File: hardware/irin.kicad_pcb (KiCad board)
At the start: 2 copper layers, 12 parts, among them J1 Battery terminals, U1 MP1584EN set to 5.0V, U2 01Space ESP32-C3-0.42LCD, U3 HiLetgo ADS1115 (0x48, ADDR->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, U4 DHT-22

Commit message: Rename project to Irin
Irin (Aramaic ʿirin, "watchers", "the wakeful ones") from the Book of
Enoch; the name's root is documented in README.md and CLAUDE.md.

- KiCad project hardware/irin.*, footprint library Uncharted -> Irin;
  ERC unchanged, regenerated netlist equivalent, preview.pdf refreshed
- Firmware config esphome/irin.yaml, dashboard ha_config/dashboard.yaml
- Breadboard generator points at irin.net; regenerated, validates OK
- The "Uncharted 12V" instance keeps its device name, entity IDs and
  secrets keys so existing HA entities and history are untouched

Co-Authored-By: Claude Opus 5.5 <noreply@anthropic.com>
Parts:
- U1: footprint Uncharted:MP1584EN_HW133_2x2Pad_P2.54mm_W7.62mm_L17.78mm -> Irin:MP1584EN_HW133_2x2Pad_P2.54mm_W7.62mm_L17.78mm
- U2: footprint Uncharted:ESP32C3_042LCD_2x8_P2.54mm_W17.78mm -> Irin:ESP32C3_042LCD_2x8_P2.54mm_W17.78mm
- U3: footprint Uncharted:ADS1115_HiLetgo_1x10_P2.54mm_W18mm_L28.3mm -> Irin:ADS1115_HiLetgo_1x10_P2.54mm_W18mm_L28.3mm
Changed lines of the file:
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@@
 		)
 	)
-	(footprint "Uncharted:MP1584EN_HW133_2x2Pad_P2.54mm_W7.62mm_L17.78mm"
+	(footprint "Irin:MP1584EN_HW133_2x2Pad_P2.54mm_W7.62mm_L17.78mm"
 		(layer "F.Cu")
 		(at 22.987 64.8208)
-		(descr "MP1584EN adjustable buck module, HW-133A~F clone (silkscreen: 降压模块 / 输入 / 输出). 4 nets, each broken out to 2 redundant through-holes at 0.1in pitch: VIN-/VIN+ on one edge, VOUT-/VOUT+ on the opposite edge, 0.7in apart; the two net pairs on each edge are 0.3in apart center-to-center. Measured by owner with a ruler (input/output edge spacing and pair pitch only -- +/-0.5mm). Board outline below is NOT measured -- it is a generous placeholder box around the hole pattern for visual reference only. Pad numbers match the Uncharted:BUCK_MODULE schematic symbol (1=IN+ 2=IN- 3=OUT+ 4=OUT-). Rectangular pads mark the '+' nets (IN+, OUT+), matching the square pads printed on the real board next to its own '+' silkscreen -- also serves as the footprint's pin-1 indicator.")
+		(descr "MP1584EN adjustable buck module, HW-133A~F clone (silkscreen: 降压模块 / 输入 / 输出). 4 nets, each broken out to 2 redundant through-holes at 0.1in pitch: VIN-/VIN+ on one edge, VOUT-/VOUT+ on the opposite edge, 0.7in apart; the two net pairs on each edge are 0.3in apart center-to-center. Measured by owner with a ruler (input/output edge spacing and pair pitch only -- +/-0.5mm). Board outline below is NOT measured -- it is a generous placeholder box around the hole pattern for visual reference only. Pad numbers match the Irin:BUCK_MODULE schematic symbol (1=IN+ 2=IN- 3=OUT+ 4=OUT-). Rectangular pads mark the '+' nets (IN+, OUT+), matching the square pads printed on the real board next to its own '+' silkscreen -- also serves as the footprint's pin-1 indicator.")
 		(tags "MP1584EN HW-133 buck module perfboard")
 		(property "Reference" "U1"
@@
 		)
 		(sheetname "/")
-		(sheetfile "uncharted-battery-monitor.kicad_sch")
+		(sheetfile "irin.kicad_sch")
 		(units
 			(unit
@@
 		)
 		(sheetname "/")
-		(sheetfile "uncharted-battery-monitor.kicad_sch")
+		(sheetfile "irin.kicad_sch")
 		(units
 			(unit
@@
 		)
 	)
-	(footprint "Uncharted:ESP32C3_042LCD_2x8_P2.54mm_W17.78mm"
+	(footprint "Irin:ESP32C3_042LCD_2x8_P2.54mm_W17.78mm"
 		(layer "F.Cu")
 		(at 34.5948 57.2008)
-		(descr "01Space ESP32-C3-0.42LCD dev board: 2x8 THT pin rows, 0.1in pitch, 0.7in row spacing. Pad numbers match the Uncharted:ESP32C3_BOARD schematic symbol (1=5V 2=3V3 3=GND 4=GPIO3 5=GPIO5 6=GPIO6); pads 7-16 are the board's other physical pins, not used in this design, numbered arbitrarily.")
+		(descr "01Space ESP32-C3-0.42LCD dev board: 2x8 THT pin rows, 0.1in pitch, 0.7in row spacing. Pad numbers match the Irin:ESP32C3_BOARD schematic symbol (1=5V 2=3V3 3=GND 4=GPIO3 5=GPIO5 6=GPIO6); pads 7-16 are the board's other physical pins, not used in this design, numbered arbitrarily.")
 		(tags "ESP32-C3 01Space 0.42LCD perfboard")
 		(property "Reference" "U2"
@@
 		)
 		(sheetname "/")
-		(sheetfile "uncharted-battery-monitor.kicad_sch")
+		(sheetfile "irin.kicad_sch")
 		(units
 			(unit
@@
 		)
 		(sheetname "/")
-		(sheetfile "uncharted-battery-monitor.kicad_sch")
+		(sheetfile "irin.kicad_sch")
 		(units
 			(unit
@@
 		)
 		(sheetname "/")
-		(sheetfile "uncharted-battery-monitor.kicad_sch")
+		(sheetfile "irin.kicad_sch")
 		(units
 			(unit
@@
 		)
 		(sheetname "/")
-		(sheetfile "uncharted-battery-monitor.kicad_sch")
+		(sheetfile "irin.kicad_sch")
 		(units
 			(unit
@@
 		)
 	)
-	(footprint "Uncharted:ADS1115_HiLetgo_1x10_P2.54mm_W18mm_L28.3mm"
+	(footprint "Irin:ADS1115_HiLetgo_1x10_P2.54mm_W18mm_L28.3mm"
 		(layer "F.Cu")
 		(at 70.9732 63.0682 -90)
-		(descr "HiLetgo ADS1115 16-bit ADC breakout (ASIN B07VPFLSMX). Single row of 10 THT pins at 0.1in (2.54mm) pitch along one long edge. Board outline 28.3mm x 18mm is from the published listing spec, NOT measured by owner -- drawn as a generous placeholder box for visual reference only, same caveat as Uncharted:MP1584EN_HW133. Pin ROW ORDER is CONFIRMED by owner against the physical module's silkscreen as VDD GND SCL SDA ADDR ALRT A0 A1 A2 A3 (left to right). Pad numbers match the Uncharted:ADS1115 schematic symbol (1=VDD 2=GND 3=SCL 4=SDA 5=ADDR 6=A0); pads 7,9,10 are the module's other physical pins (ALRT, A1, A2, A3) not used in this design, numbered arbitrarily. The module is cable-wired to the ESP32's Qwiic port rather than pin-header-mounted (see CLAUDE.md).")
+		(descr "HiLetgo ADS1115 16-bit ADC breakout (ASIN B07VPFLSMX). Single row of 10 THT pins at 0.1in (2.54mm) pitch along one long edge. Board outline 28.3mm x 18mm is from the published listing spec, NOT measured by owner -- drawn as a generous placeholder box for visual reference only, same caveat as Irin:MP1584EN_HW133. Pin ROW ORDER is CONFIRMED by owner against the physical module's silkscreen as VDD GND SCL SDA ADDR ALRT A0 A1 A2 A3 (left to right). Pad numbers match the Irin:ADS1115 schematic symbol (1=VDD 2=GND 3=SCL 4=SDA 5=ADDR 6=A0); pads 7,9,10 are the module's other physical pins (ALRT, A1, A2, A3) not used in this design, numbered arbitrarily. The module is cable-wired to the ESP32's Qwiic port rather than pin-header-mounted (see CLAUDE.md).")
 		(tags "ADS1115 HiLetgo ADC breakout perfboard")
 		(property "Reference" "U3"
@@
 		)
 		(sheetname "/")
-		(sheetfile "uncharted-battery-monitor.kicad_sch")
+		(sheetfile "irin.kicad_sch")
 		(units
 			(unit
@@
 		)
 		(sheetname "/")
-		(sheetfile "uncharted-battery-monitor.kicad_sch")
+		(sheetfile "irin.kicad_sch")
 		(units
 			(unit
@@
 		)
 		(sheetname "/")
-		(sheetfile "uncharted-battery-monitor.kicad_sch")
+		(sheetfile "irin.kicad_sch")
 		(units
 			(unit
@@
 		)
 		(sheetname "/")
-		(sheetfile "uncharted-battery-monitor.kicad_sch")
+		(sheetfile "irin.kicad_sch")
 		(units
 			(unit
@@
 		)
 		(sheetname "/")
-		(sheetfile "uncharted-battery-monitor.kicad_sch")
+		(sheetfile "irin.kicad_sch")
 		(units
 			(unit
@@
 		)
 		(sheetname "/")
-		(sheetfile "uncharted-battery-monitor.kicad_sch")
+		(sheetfile "irin.kicad_sch")
 		(units
 			(unit

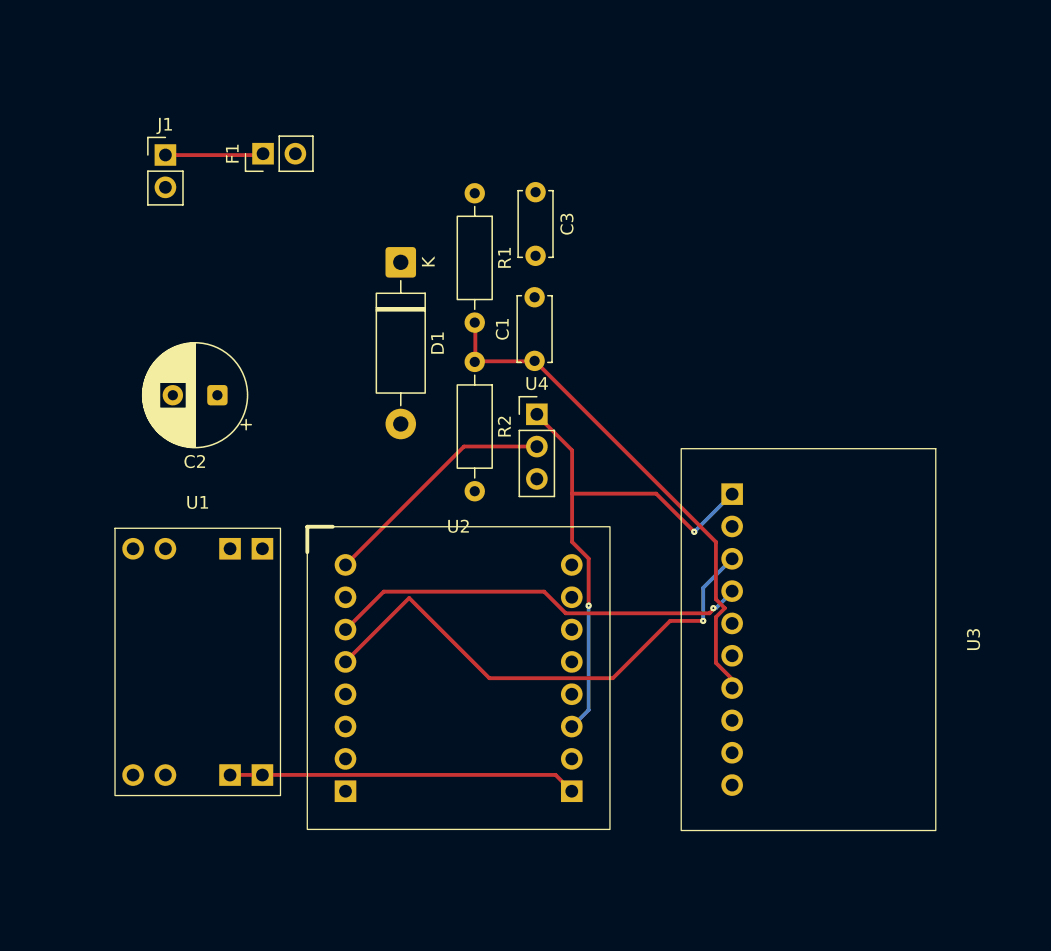
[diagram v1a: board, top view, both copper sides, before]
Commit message: Hardware: conventional schematic symbols; PCB outline, placement, GND plane, routing
Schematic (netlist unchanged):
- ANSI resistors, two-plate caps, TVS with cathode bar, fuse, battery (J1)
- Detailed ESP32-C3, ADS1115 and DHT22 symbols; U2 3V3 top / GND bottom,
  U1 outputs on the right

PCB:
- Board outline 78.5 x 69 mm, four M3 mounting holes inset 3.5 mm
- Parts re-placed, C3 at the buck input, divider beside the ADS1115
- B.Cu GND plane with thermal reliefs; "Pwr" net class (0.4 mm) for 12vPROT
- Fully routed: DRC 0 violations, 0 unconnected, 0 schematic parity issues

Regenerated preview.pdf and irin.net.

Co-Authored-By: Claude Opus 5.5 <noreply@anthropic.com>
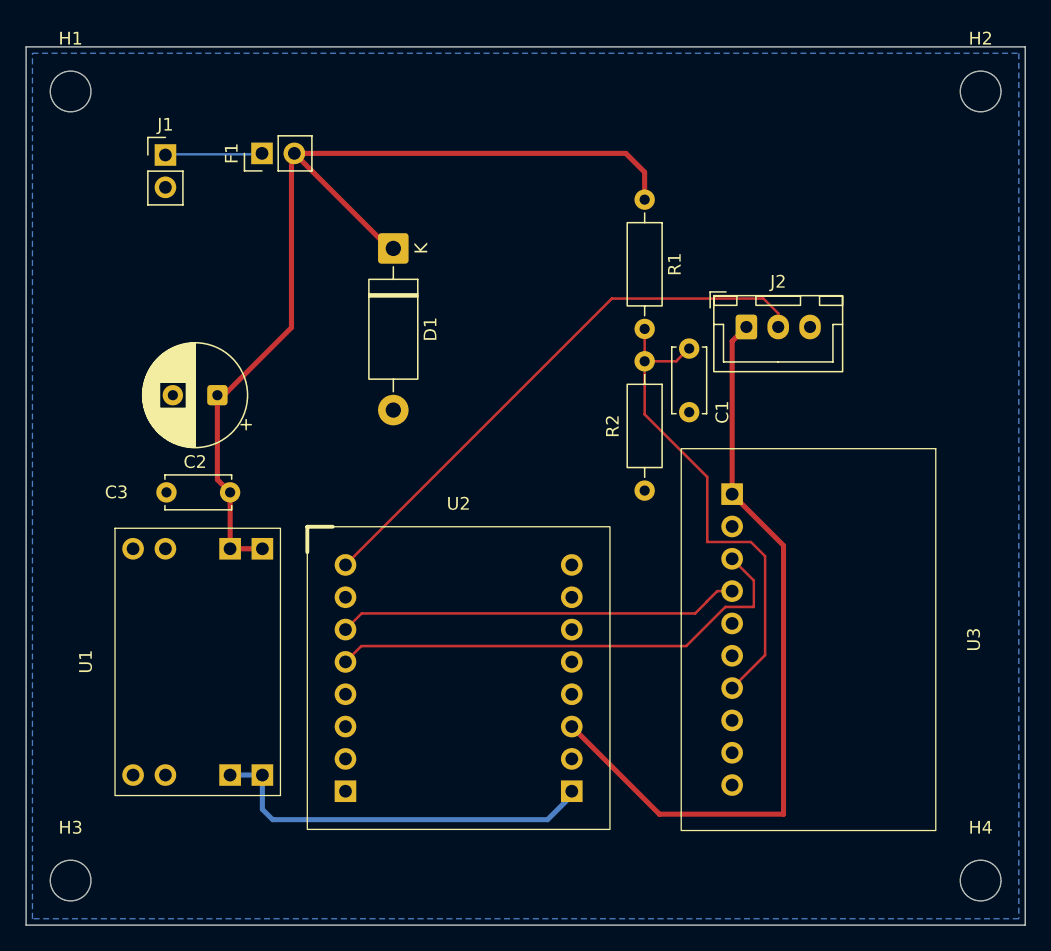
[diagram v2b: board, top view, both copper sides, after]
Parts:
- added H1: MountingHole_3.2mm_M3, MountingHole_3.2mm_M3, F.Cu at (13.0, 20.0)
- added H2: MountingHole_3.2mm_M3, MountingHole_3.2mm_M3, F.Cu at (84.5, 20.0)
- added H3: MountingHole_3.2mm_M3, MountingHole_3.2mm_M3, F.Cu at (13.0, 82.0)
- added H4: MountingHole_3.2mm_M3, MountingHole_3.2mm_M3, F.Cu at (84.5, 82.0)
- C1: value 0.1uF -> 2nF mica (2x1000pF)
- J2: renamed from U4; value DHT-22 -> DHT22 remote (VCC/DATA/GND); footprint Connector_PinHeader_2.54mm:PinHeader_1x03_P2.54mm_Vertical -> Connector_JST:JST_XH_B3B-XH-A_1x03_P2.50mm_Vertical
- R1: value 470k 1% -> 47k 1%
- R2: value 100k 1% -> 10k 1%
- moved C3 33.6 mm to (25.5, 51.5), turned to 180 degrees
- moved J2 17.8 mm to (66.1, 38.5)
- moved R1 13.4 mm to (58.1, 28.5)
- moved R2 13.4 mm to (58.1, 41.2)
- moved C1 12.2 mm to (61.6, 40.2), turned to -90 degrees
- moved D1 1.24 mm to (38.4, 32.3)
- moved F1 0.09 mm to (28.0, 24.9)
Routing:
- net /12vPROT: track 0.00 -> 78.2 mm
- net Net-(J2-DATA): track 18.9 -> 44.2 mm
- net Net-(J2-VCC): track 41.8 -> 59.9 mm, vias 2 -> 0
- net Net-(U1-OUT+): track 27.4 -> 31.0 mm
- net Net-(U2-GPIO6): track 40.5 -> 38.4 mm, vias 1 -> 0
- net Net-(U2-GPIO5): track 33.0 -> 31.6 mm, vias 1 -> 0
- net Net-(U3-A0): track 40.4 -> 39.5 mm
- added copper zone on B.Cu, net /GND
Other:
- board outline added: 78.5 x 69 mm

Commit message: Hardware rev B: swap buck and ADC sides, reroute, antenna keepout
- U1 (MP1584) and U3 (ADS1115) swapped so each sits beside the U2 pins it
  serves; input parts (J1, D1, C3, C2) moved to the right/top, 12 V now a
  straight drop to U1. All routing on F.Cu; B.Cu is an unbroken GND plane
  apart from a rule-area keepout under U2's antenna end. No vias.
  DRC 0 / unconnected 0 / parity clean.
- Schematic: F1 is the inline harness fuse (excluded from board, kept in
  BOM); BT1 (vehicle battery, off-board) added inside a dashed
  "OFF-BOARD (vehicle harness)" box. J1 redrawn as a 2-pin connector.
  J2 and divider notes updated (DHT22 inside for now; PCB divider ground
  goes straight to the plane). ERC: only the 12 library-config warnings.
- CLAUDE.md: USB-end margin kept for lid-off cable access, antenna end,
  J1 position for the enclosure model.

Co-Authored-By: Claude Opus 5.5 <noreply@anthropic.com>
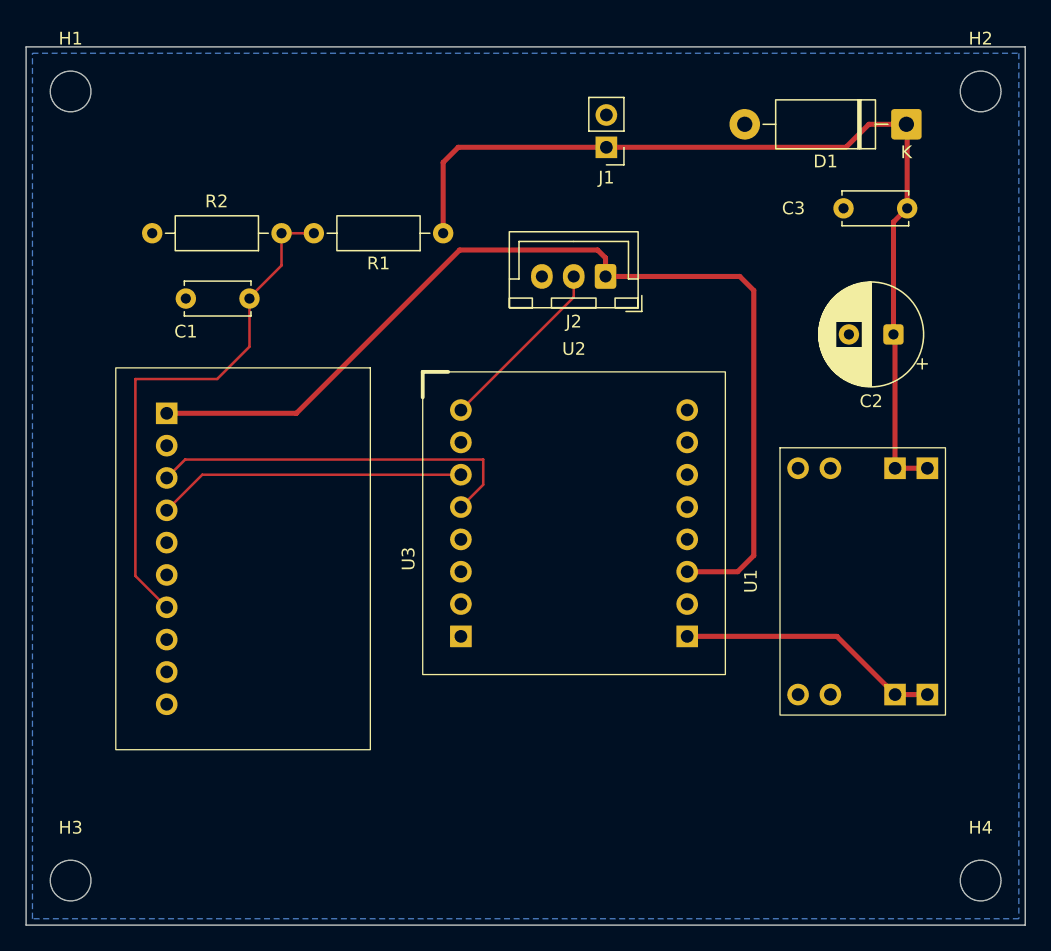
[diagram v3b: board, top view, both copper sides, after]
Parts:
- removed F1: 5A (Micro2 blade), Connector_PinHeader_2.54mm:PinHeader_1x02_P2.54mm_Vertical
- moved C3 57.7 mm to (78.7, 29.2)
- moved C2 53.3 mm to (77.6, 39.1)
- moved U1 52.6 mm to (75.2, 58.5)
- moved U3 44.9 mm to (26.5, 56.7)
- moved D1 41.5 mm to (78.7, 22.6), turned to 180 degrees
- moved C1 34.8 mm to (27.1, 36.3), turned to 180 degrees
- moved J1 34.7 mm to (55.1, 24.4), turned to 180 degrees
- moved R2 30.3 mm to (29.6, 31.1), turned to 180 degrees
- moved R1 16.0 mm to (42.3, 31.1), turned to 180 degrees
- moved U2 15.2 mm to (43.7, 45.0)
- moved J2 11.8 mm to (55.0, 34.5), turned to 180 degrees
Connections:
- J1 pad 1: Net-(J1-BATT+) -> /12vPROT
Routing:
- net Net-(J2-DATA): track 44.2 -> 14.2 mm
- net Net-(J2-VCC): track 59.9 -> 80.2 mm
- net Net-(U1-OUT+): track 31.0 -> 20.8 mm
- net Net-(U2-GPIO6): track 38.4 -> 29.9 mm
- net Net-(J1-BATT+): track 7.82 -> 0.00 mm
- net Net-(U2-GPIO5): track 31.6 -> 24.3 mm
- net /12vPROT: track 78.2 -> 73.0 mm
- net Net-(U3-A0): track 39.5 -> 41.4 mm

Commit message: Hardware rev B: screw-terminal J1, full silkscreen, D1 standard
- J1: 5.08 mm 2-pin screw terminal (Phoenix MKDS 1,5-2-5.08 footprint,
  KF301-2P fits) at the top edge, wire openings facing out; replaces the
  2.54 mm header, which neither takes 18 AWG nor survives vibration.
- Silkscreen for kit builders: part values on every part, J1 +/-, J2
  VCC/DATA/GND, U1 IN/OUT, U2 used pins and USB-C end, U3 pin names,
  "Irin - by AI7MG - rev B". Values shortened to fit (C1, J2, U3, J1).
  Mounting-hole references hidden.
- D1 (P6KE18A) fitted as standard: it also acts as the reverse-polarity
  crowbar (reversed hookup forward-biases D1 and blows F1). Schematic
  notes, CLAUDE.md, PARTS.md and README updated.
- DRC: 0 errors; one silkscreen-clearance warning where the USB-C mark
  meets U2's outline, intentionally. ERC: the 12 library-config warnings.

Co-Authored-By: Claude Opus 5.5 <noreply@anthropic.com>
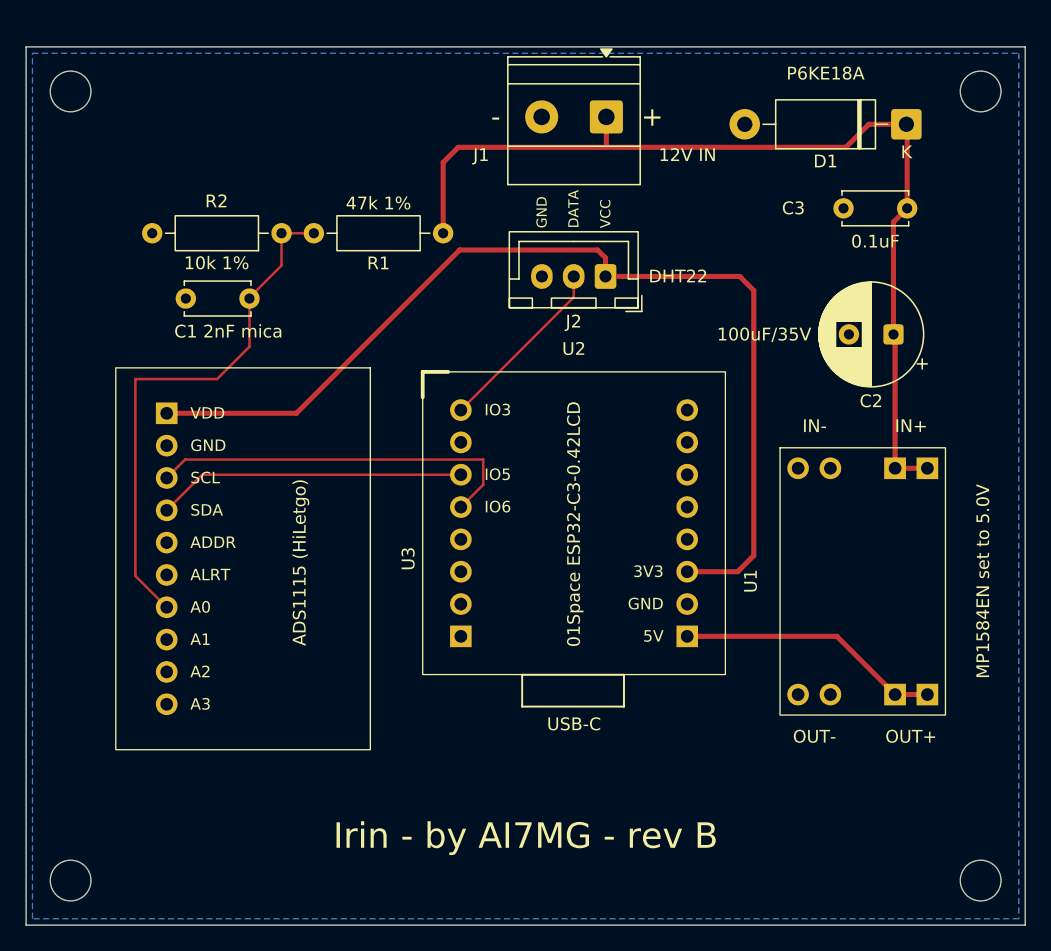
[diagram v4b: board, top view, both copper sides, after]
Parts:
- C1: value 2nF mica (2x1000pF) -> 2nF mica
- D1: value P6KE18A (opt.) -> P6KE18A
- J1: value Battery terminals -> 12V IN; footprint Connector_PinHeader_2.54mm:PinHeader_1x02_P2.54mm_Vertical -> TerminalBlock_Phoenix:TerminalBlock_Phoenix_MKDS-1,5-2-5.08_1x02_P5.08mm_Horizontal
- J2: value DHT22 remote (VCC/DATA/GND) -> DHT22
- U3: value HiLetgo ADS1115 (0x48, ADDR->GND) -> ADS1115 (HiLetgo)
- moved J1 2.39 mm to (55.1, 22.0)
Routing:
- net /12vPROT: track 73.0 -> 75.4 mm
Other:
- board text added: "+"
- board text added: "-"
- board text added: "3V3"
- board text added: "5V"
- board text added: "A0"
- board text added: "A1"
- board text added: "A2"
- board text added: "A3"
- board text added: "ADDR"
- board text added: "ALRT"
- board text added: "DATA"
- board text added: "GND"
- board text added: "IN+"
- board text added: "IN-"
- board text added: "IO3"
- board text added: "IO5"
- board text added: "IO6"
- board text added: "Irin - by AI7MG - rev B"
- board text added: "OUT+"
- board text added: "OUT-"
- board text added: "SCL"
- board text added: "SDA"
- board text added: "USB-C"
- board text added: "VCC"
- board text added: "VDD"
